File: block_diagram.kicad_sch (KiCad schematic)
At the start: 0 parts

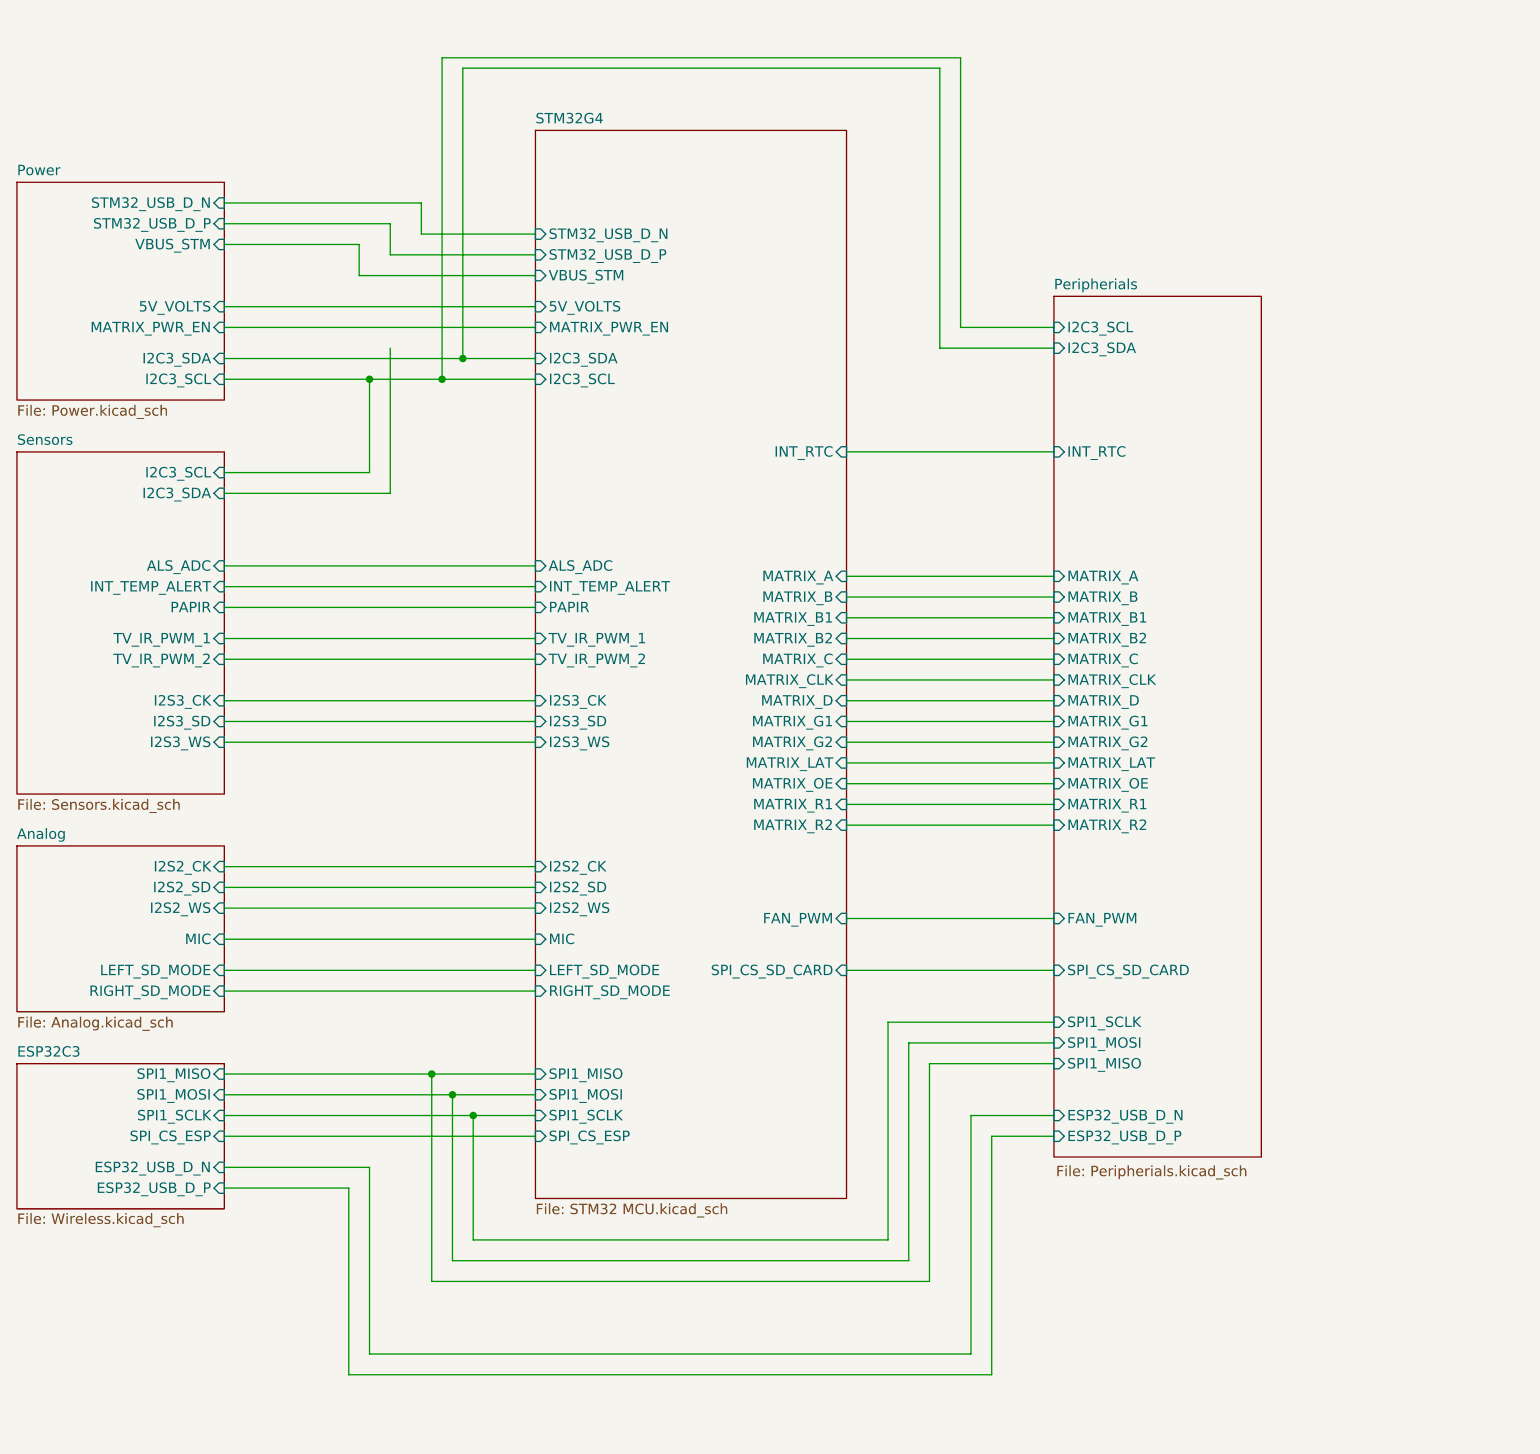
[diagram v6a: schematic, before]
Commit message: fixing block diagram, adding 5v detect, removing flag pin
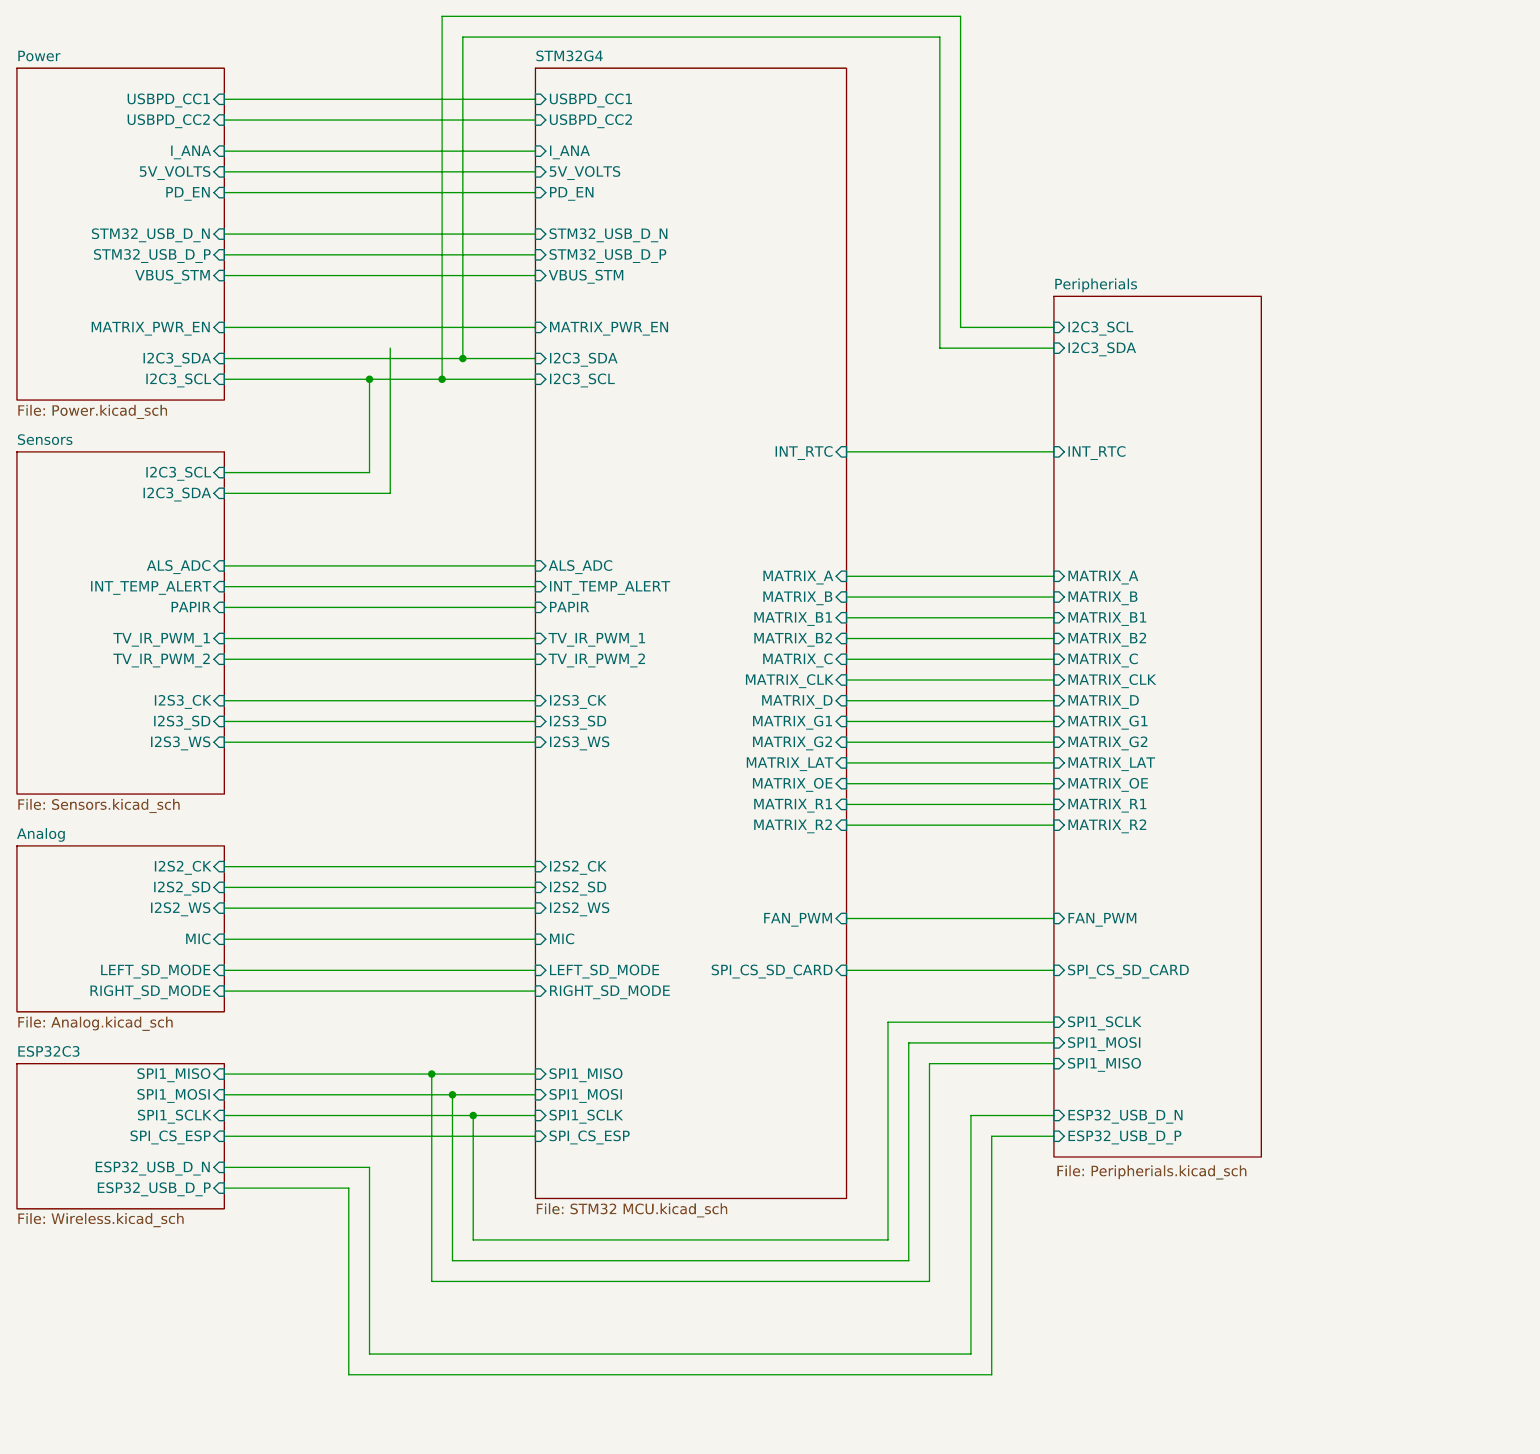
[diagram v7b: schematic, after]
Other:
- sheet Power ports: added I_ANA, PD_EN, USBPD_CC1, USBPD_CC2; removed none
- sheet STM32G4 ports: added I_ANA, PD_EN, USBPD_CC1, USBPD_CC2; removed none
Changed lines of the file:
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@@
 	(wire
 		(pts
-			(xy 93.98 21.59) (xy 93.98 57.15)
+			(xy 93.98 17.78) (xy 93.98 57.15)
 		)
 		(stroke
@@
 	(wire
 		(pts
-			(xy 152.4 21.59) (xy 93.98 21.59)
+			(xy 64.77 31.75) (xy 102.87 31.75)
+		)
+		(stroke
+			(width 0)
+			(type default)
+		)
+	)
+	(wire
+		(pts
+			(xy 152.4 17.78) (xy 93.98 17.78)
 		)
 		(stroke
@@
 	(wire
 		(pts
-			(xy 154.94 53.34) (xy 154.94 20.32)
+			(xy 154.94 53.34) (xy 154.94 15.24)
 		)
 		(stroke
@@
 	(wire
 		(pts
-			(xy 85.09 44.45) (xy 102.87 44.45)
-		)
-		(stroke
-			(width 0)
-			(type default)
-		)
-	)
-	(wire
-		(pts
-			(xy 64.77 43.18) (xy 81.28 43.18)
-		)
-		(stroke
-			(width 0)
-			(type default)
-		)
-	)
-	(wire
-		(pts
-			(xy 91.44 20.32) (xy 91.44 59.69)
-		)
-		(stroke
-			(width 0)
-			(type default)
-		)
-	)
-	(wire
-		(pts
-			(xy 64.77 40.64) (xy 85.09 40.64)
+			(xy 64.77 46.99) (xy 102.87 46.99)
+		)
+		(stroke
+			(width 0)
+			(type default)
+		)
+	)
+	(wire
+		(pts
+			(xy 91.44 15.24) (xy 91.44 59.69)
+		)
+		(stroke
+			(width 0)
+			(type default)
+		)
+	)
+	(wire
+		(pts
+			(xy 64.77 44.45) (xy 102.87 44.45)
 		)
 		(stroke
@@
 	(wire
 		(pts
-			(xy 81.28 46.99) (xy 102.87 46.99)
-		)
-		(stroke
-			(width 0)
-			(type default)
-		)
-	)
-	(wire
-		(pts
 			(xy 151.13 143.51) (xy 151.13 170.18)
 		)
@@
 	(wire
 		(pts
+			(xy 64.77 34.29) (xy 102.87 34.29)
+		)
+		(stroke
+			(width 0)
+			(type default)
+		)
+	)
+	(wire
+		(pts
 			(xy 82.55 179.07) (xy 82.55 156.21)
 		)
@@
 	(wire
 		(pts
-			(xy 102.87 41.91) (xy 88.9 41.91)
-		)
-		(stroke
-			(width 0)
-			(type default)
-		)
-	)
-	(wire
-		(pts
 			(xy 64.77 71.12) (xy 82.55 71.12)
 		)
@@
 	(wire
 		(pts
+			(xy 64.77 27.94) (xy 102.87 27.94)
+		)
+		(stroke
+			(width 0)
+			(type default)
+		)
+	)
+	(wire
+		(pts
 			(xy 64.77 119.38) (xy 102.87 119.38)
 		)
@@
 	(wire
 		(pts
-			(xy 64.77 38.1) (xy 88.9 38.1)
+			(xy 64.77 25.4) (xy 102.87 25.4)
+		)
+		(stroke
+			(width 0)
+			(type default)
+		)
+	)
+	(wire
+		(pts
+			(xy 64.77 41.91) (xy 102.87 41.91)
 		)
 		(stroke
@@
 	(wire
 		(pts
-			(xy 81.28 43.18) (xy 81.28 46.99)
+			(xy 64.77 36.83) (xy 102.87 36.83)
 		)
 		(stroke
@@
 	(wire
 		(pts
-			(xy 64.77 50.8) (xy 102.87 50.8)
-		)
-		(stroke
-			(width 0)
-			(type default)
-		)
-	)
-	(wire
-		(pts
 			(xy 146.05 165.1) (xy 146.05 138.43)
 		)
@@
 	(wire
 		(pts
-			(xy 154.94 20.32) (xy 91.44 20.32)
+			(xy 154.94 15.24) (xy 91.44 15.24)
 		)
 		(stroke
@@
 	(wire
 		(pts
-			(xy 85.09 40.64) (xy 85.09 44.45)
-		)
-		(stroke
-			(width 0)
-			(type default)
-		)
-	)
-	(wire
-		(pts
 			(xy 85.09 55.88) (xy 85.09 73.66)
 		)
@@
 	(wire
 		(pts
-			(xy 88.9 41.91) (xy 88.9 38.1)
-		)
-		(stroke
-			(width 0)
-			(type default)
-		)
-	)
-	(wire
-		(pts
 			(xy 64.77 128.27) (xy 102.87 128.27)
 		)
@@
 	(wire
 		(pts
-			(xy 152.4 55.88) (xy 152.4 21.59)
+			(xy 152.4 55.88) (xy 152.4 17.78)
 		)
 		(stroke
@@
 	)
 	(sheet
-		(at 102.87 29.21)
-		(size 38.1 130.81)
+		(at 102.87 21.59)
+		(size 38.1 138.43)
 		(exclude_from_sim no)
 		(in_bom yes)
@@
 		)
 		(property "Sheetname" "STM32G4"
-			(at 102.87 28.4984 0)
+			(at 102.87 20.8784 0)
 			(show_name no)
 			(do_not_autoplace no)
@@
 			)
 		)
-		(pin "5V_VOLTS" input
-			(at 102.87 50.8 180)
-			(effects
-				(font
-					(size 1.27 1.27)
-				)
-				(justify left)
-			)
-		)
 		(pin "ALS_ADC" input
 			(at 102.87 82.55 180)
@@
 				)
 				(justify right)
+			)
+		)
+		(pin "5V_VOLTS" input
+			(at 102.87 34.29 180)
+			(effects
+				(font
+					(size 1.27 1.27)
+				)
+				(justify left)
+			)
+		)
+		(pin "I_ANA" input
+			(at 102.87 31.75 180)
+			(effects
+				(font
+					(size 1.27 1.27)
+				)
+				(justify left)
+			)
+		)
+		(pin "PD_EN" input
+			(at 102.87 36.83 180)
+			(effects
+				(font
+					(size 1.27 1.27)
+				)
+				(justify left)
+			)
+		)
+		(pin "USBPD_CC1" input
+			(at 102.87 25.4 180)
+			(effects
+				(font
+					(size 1.27 1.27)
+				)
+				(justify left)
+			)
+		)
+		(pin "USBPD_CC2" input
+			(at 102.87 27.94 180)
+			(effects
+				(font
+					(size 1.27 1.27)
+				)
+				(justify left)
 			)
 		)
@@
 	)
 	(sheet
-		(at 39.37 35.56)
-		(size 25.4 26.67)
+		(at 39.37 21.59)
+		(size 25.4 40.64)
 		(exclude_from_sim no)
 		(in_bom yes)
@@
 		)
 		(property "Sheetname" "Power"
-			(at 39.37 34.8484 0)
+			(at 39.37 20.8784 0)
 			(show_name no)
 			(do_not_autoplace no)
@@
 			)
 		)
-		(pin "5V_VOLTS" input
-			(at 64.77 50.8 0)
-			(effects
-				(font
-					(size 1.27 1.27)
-				)
-				(justify right)
-			)
-		)
 		(pin "I2C3_SCL" input
 			(at 64.77 59.69 0)
@@
 		)
 		(pin "STM32_USB_D_N" input
-			(at 64.77 38.1 0)
+			(at 64.77 41.91 0)
 			(effects
 				(font
@@
 		)
 		(pin "STM32_USB_D_P" input
-			(at 64.77 40.64 0)
+			(at 64.77 44.45 0)
 			(effects
 				(font
@@
 		)
 		(pin "VBUS_STM" input
-			(at 64.77 43.18 0)
-			(effects
-				(font
+			(at 64.77 46.99 0)
+			(effects
+				(font
+					(size 1.27 1.27)
+				)
+				(justify right)
+			)
+		)
+		(pin "I_ANA" input
+			(at 64.77 31.75 0)
+			(effects
+				(font
+					(size 1.27 1.27)
+				)
+				(justify right)
+			)
+		)
+		(pin "PD_EN" input
+			(at 64.77 36.83 0)
+			(effects
+				(font
+					(size 1.27 1.27)
+				)
+				(justify right)
+			)
+		)
+		(pin "USBPD_CC1" input
+			(at 64.77 25.4 0)
+			(effects
+				(font
+					(size 1.27 1.27)
+				)
+				(justify right)
+			)
+		)
+		(pin "USBPD_CC2" input
+			(at 64.77 27.94 0)
+			(effects
+				(font
+					(size 1.27 1.27)
+				)
+				(justify right)
+			)
+		)
+		(pin "5V_VOLTS" input
+			(at 64.77 34.29 0)
+			(effects
+				(font
